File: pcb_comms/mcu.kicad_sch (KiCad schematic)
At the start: 24 parts, among them SW1 SW_SPDT, U2 STM32WLE5CCU6, Y3 32MHz

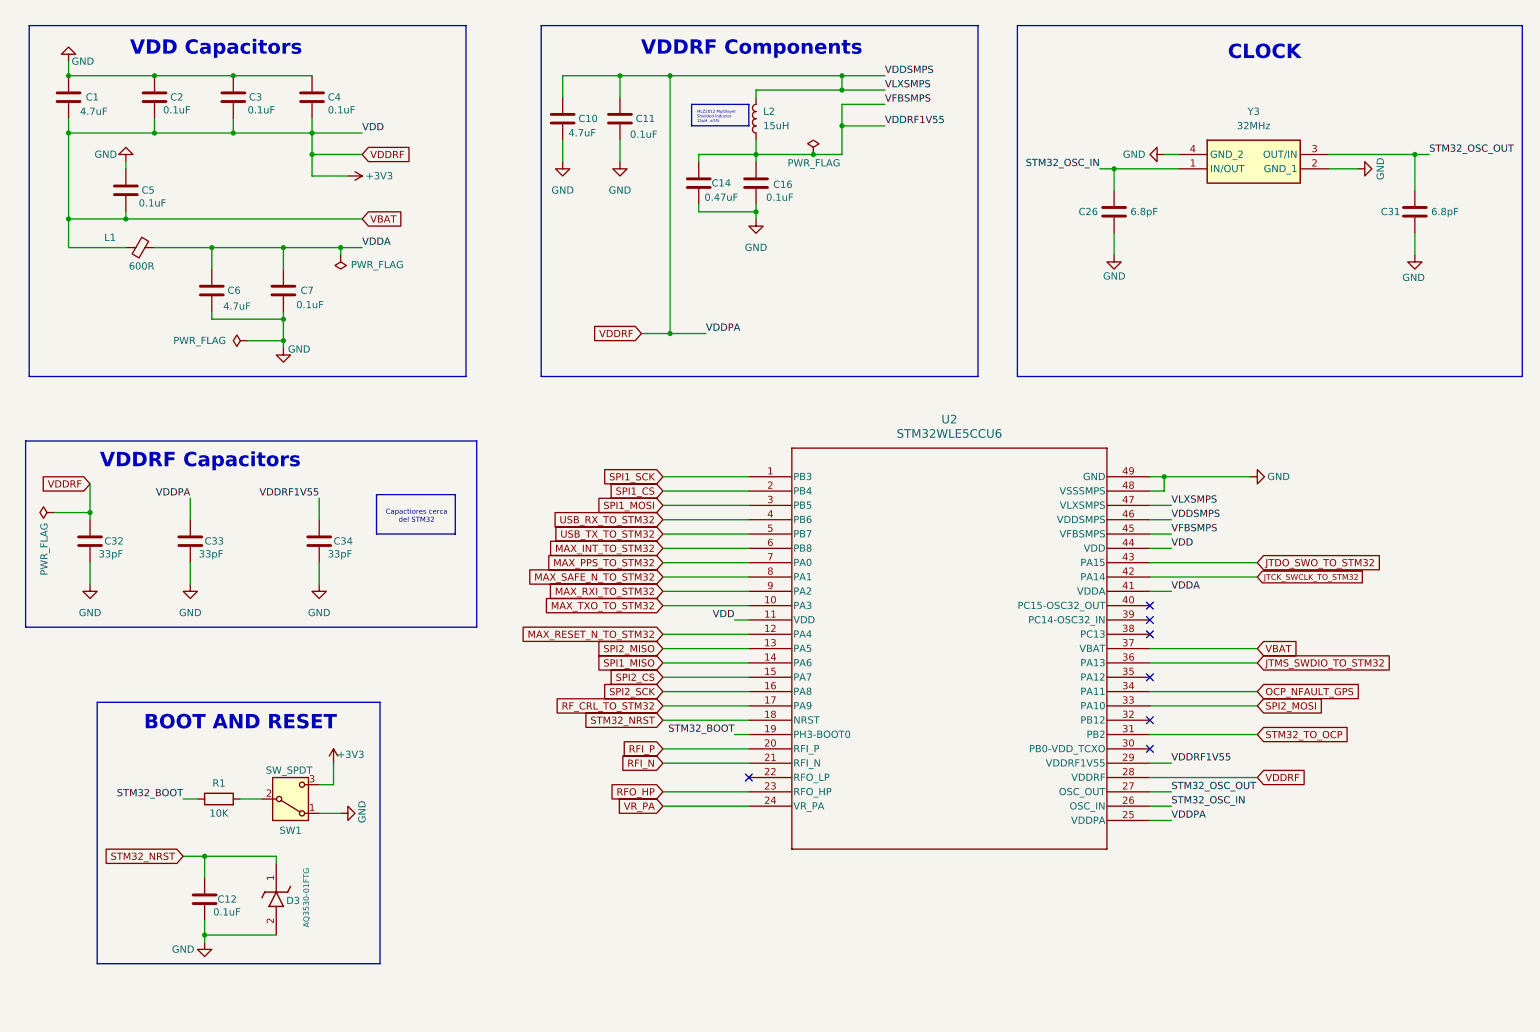
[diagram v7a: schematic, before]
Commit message: Add footprints
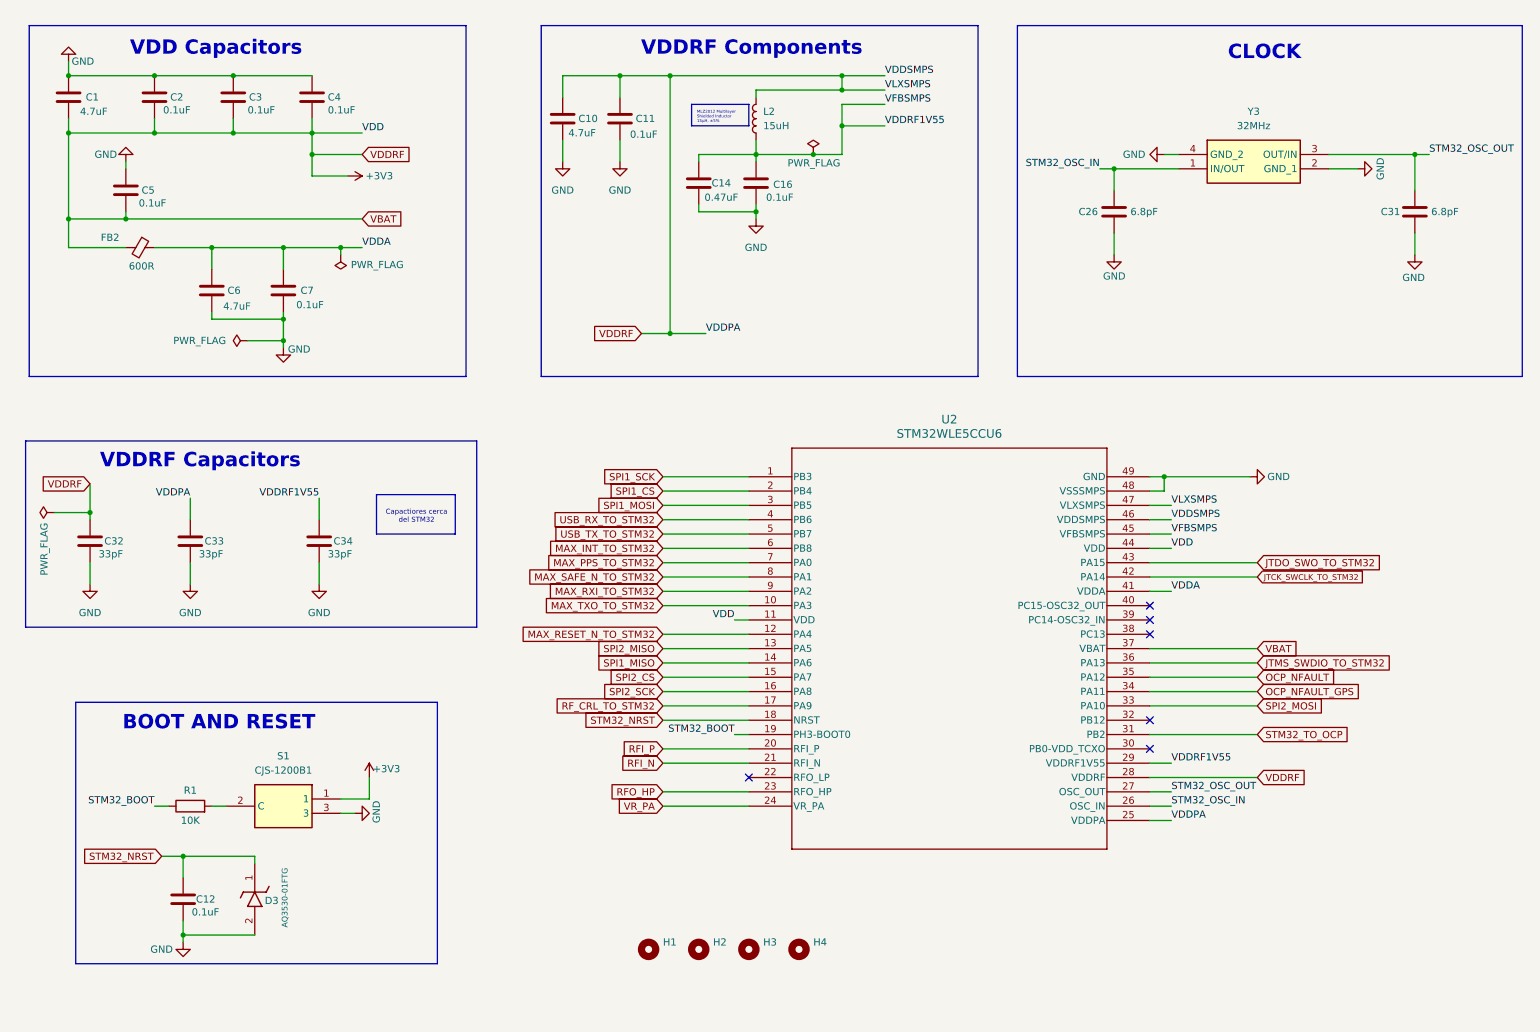
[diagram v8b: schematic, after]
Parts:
- removed SW1: SW_SPDT, symbol Switch:SW_SPDT
- added H1, H2, H3, H4: MountingHole, MountingHole:MountingHole_3.2mm_M3_Pad_Via, symbol Mechanical:MountingHole
- added S1: CJS-1200B1, SW_BOOT_CJS-1200B1:SW_BOOT_CJS-1200B1, symbol SW_BOOT_CJS-1200B1:CJS-1200B1
- C1, C10, C11, C12, C14, C16, C2, C26, C3, C31, C32, C33, C34, C4, C5, C6, C7: footprint (none) -> Capacitor_SMD:C_0805_2012Metric_Pad1.18x1.45mm_HandSolder
- D3: footprint (none) -> ESD_PROTECTION_DIODE_AQ3530-01FTG:ESD_PROTECTION_DIODE_AQ3530-01FTG
- FB2: renamed from L1; footprint (none) -> Inductor_SMD:L_1206_3216Metric_Pad1.22x1.90mm_HandSolder
- L2: footprint (none) -> Inductor_SMD:L_0805_2012Metric_Pad1.05x1.20mm_HandSolder
- R1: footprint (none) -> Resistor_SMD:R_0805_2012Metric_Pad1.20x1.40mm_HandSolder
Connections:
- net +3V3: now also S1.1
- net GND: now also S1.3
- net at R1.2: now also S1.2 (C)
- net OCP_NFAULT: now reaches U2.35 (PA12)
- no-connect marks 7 -> 6
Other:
- moved on the sheet: C12, D3, R1
